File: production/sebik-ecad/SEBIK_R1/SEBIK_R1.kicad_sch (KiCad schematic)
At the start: 59 parts

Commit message: updated schematic with usb port, test points, and mounting holes
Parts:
- removed FB? (x6): FerriteBead, symbol Device:FerriteBead
- removed J? (x2): Conn_01x02_Male, Connector_JST:JST_XH_B2B-XH-AM_1x02_P2.50mm_Vertical, symbol Connector:Conn_01x02_Male
- added C?: 100n, Capacitor_SMD:C_0805_2012Metric, symbol Device:C_Small
- added D? (x2): LED_Small, LED_SMD:LED_0805_2012Metric, symbol Device:LED_Small
- added E1, E2, E3, E4, E5, E6: MI0805K400R-10, MI0805K400R-10:FB_MI0805K400R-10, symbol MI0805K400R-10:MI0805K400R-10
- added F?: 500mA, Fuse:Fuse_1210_3225Metric, symbol Device:Fuse
- added H1, H2, H3, H4: MountingHole, MountingHole:MountingHole_3.2mm_M3, symbol Mechanical:MountingHole
- added J8, J9: Conn_01x01_Male, Connector_JST:JST_XH_B1B-XH-AM_1x01_P2.50mm_Vertical, symbol Connector:Conn_01x01_Male
- added J?: USB_B, Connector_USB:USB_Micro-B_Amphenol_10104110_Horizontal, symbol Connector:USB_B
- added R?: 10k, Resistor_SMD:R_0805_2012Metric, symbol Device:R_Small
- added R? (x5): 1k, Resistor_SMD:R_0805_2012Metric, symbol Device:R_Small
- added TP? (x2): TestPoint, TestPoint:TestPoint_Loop_D1.80mm_Drill1.0mm_Beaded, symbol Connector:TestPoint
- added U3: USBLC6-2SC6, Package_TO_SOT_SMD:SOT-23-6, symbol Power_Protection:USBLC6-2SC6
- added U4: FT232RL, Package_SO:SSOP-28_5.3x10.2mm_P0.65mm, symbol Interface_USB:FT232RL
- D?: footprint Diode_THT:D_DO-35_SOD27_P7.62mm_Horizontal -> Diode_SMD:D_0805_2012Metric
- D?: footprint (none) -> Diode_SMD:D_0805_2012Metric
- gave numbers to parts that had none: 17
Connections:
- net +5V: now also R?.1, R?.2, R?.2, TP?.1, U4.20 (VCC), U4.4 (VCCIO)
- net GND: now also C?.2, J?.4 (GND), R?.1, U3.2 (GND), U4.18 (GND), U4.21 (GND), U4.25 (AGND), U4.26 (TEST), U4.7 (GND)
- net at C?.1, U7.2 (T-): now also E5.2
- net at C?.2, U7.3 (T+): now also E6.2
- net at J5.1 (Pin_1): now also E1.1
- net at J5.2 (Pin_2): now also E2.1
- net at C?.2, U5.3 (T+): now also E2.2
- net at C?.1, U5.2 (T-): now also E1.2
- net at Q2.3 (D): now also J8.1 (Pin_1)
- net RX: now reaches U1.30 (PD0)
- net RX: now also R?.2
- net TX: now reaches U1.31 (PD1)
- net TX: now also R?.2
- net at J10.1 (Pin_1): now also E5.1
- net at Q1.3 (D): now also J9.1 (Pin_1)
- net at J6.1 (Pin_1): now also E3.1
- net at C?.1, U6.2 (T-): now also E3.2
- net at C?.2, U6.3 (T+): now also E4.2
- net at J6.2 (Pin_2): now also E4.1
- net at J10.2 (Pin_2): now also E6.1
- new net: R?.2, U4.19 (~{RESET})
- new net: D?.2 (A), R?.1 (x2)
- new net: R?.1, U4.1 (TXD)
- new net: D?.1 (K), U4.22 (CBUS1)
- new net: D?.1 (K), U4.23 (CBUS0)
- new net: R?.1, U4.5 (RXD)
- new net: F?.1, J?.1 (VBUS)
- new net +3V3: C?.1, TP?.1, U4.17 (3V3OUT)
- new net DTR: R?.2, U4.2 (DTR)
- new net USB_CON_D+: J?.3 (D+), U3.1 (I/O1)
- new net USB_CON_D-: J?.2 (D-), U3.3 (I/O2)
- new net USB_D+: U3.6 (I/O1), U4.15 (USBD+)
- new net USB_D-: U3.4 (I/O2), U4.16 (USBD-)
- new net VBUS: F?.2, U3.5 (VBUS)
- no-connect marks 0 -> 11
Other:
- note added: "GPIO Expander"
- note added: "MOUNTING HOLES"
- note added: "Microcontroller"
- note added: "USB"
- moved on the sheet: C?, D?, J1, J10, J11, J2, J3, J4, J5, J6, J7, J?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

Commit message: added non power net test points, numbered all parts and added crystal and switch footprints
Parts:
- removed D?: LED, LED_SMD:LED_0805_2012Metric, symbol Device:LED
- removed J?: 0, symbol test:3pin-I/O
- removed R?: 10k, Resistor_SMD:R_0805_2012Metric, symbol Device:R_Small
- removed R? (x5): 1k, Resistor_SMD:R_0805_2012Metric, symbol Device:R_Small
- removed R?: 1K, Resistor_SMD:R_0805_2012Metric, symbol Device:R_US
- added J12: Conn_01x02_Male, Connector_JST:JST_XH_B2B-XH-AM_1x02_P2.50mm_Vertical, symbol Connector:Conn_01x02_Male
- added R10, R11, R12, R13, R14: 1K, Resistor_SMD:R_0805_2012Metric, symbol Device:R_US
- added R9: 10k, Resistor_SMD:R_0805_2012Metric, symbol Device:R_US
- added TP_MISO, TP_SCK, TP_ej_press, TP_ej_sol_in, TP_inj_press, TP_inj_sol_in, TP_speaker: TestPoint, TestPoint:TestPoint_Loop_D1.80mm_Drill1.0mm_Beaded, symbol Connector:TestPoint
- SW?: footprint (none) -> Button_Switch_SMD:SW_SPDT_PCM12
- Y1: renamed from Y?; footprint (none) -> Crystal:Crystal_SMD_2012-2Pin_2.0x1.2mm
- gave numbers to parts that had none: 33
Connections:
- net +5V: now also R13.2, R14.2, R9.2
- net DTR: now also R12.2
- net GND: now also R12.1
- net RX: now also R11.1
- net SCK: now also TP_SCK.1
- net Speaker: now also TP_speaker.1
- net TX: now also R10.1
- net ej_press: now also TP_ej_press.1
- net ej_sol_in: now also TP_ej_sol_in.1
- net inj_press: now also TP_inj_press.1
- net inj_sol_in: now also TP_inj_sol_in.1
- net at U4.19 (~{RESET}): now also R9.1
- net at D7.2 (A): now also R13.1
- net at U4.1 (TXD): now also R10.2
- net at D8.2 (A): now also R14.1
- net at U4.5 (RXD): now also R11.2
- net at K?.14: now also J12.2 (Pin_2)
- net at K?.7, K?.8: now also J12.1 (Pin_1)
- net MISO: now reaches U1.16 (PB4)
- net MISO: now also U5.7 (SO), U6.7 (SO), U7.7 (SO), TP_MISO.1
- removed net MOSI: U1.15 (PB3), U5.7 (SO), U6.7 (SO), U7.7 (SO)
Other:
- note added: "2012"
- moved on the sheet: D7, D8, Q3, R7, R8

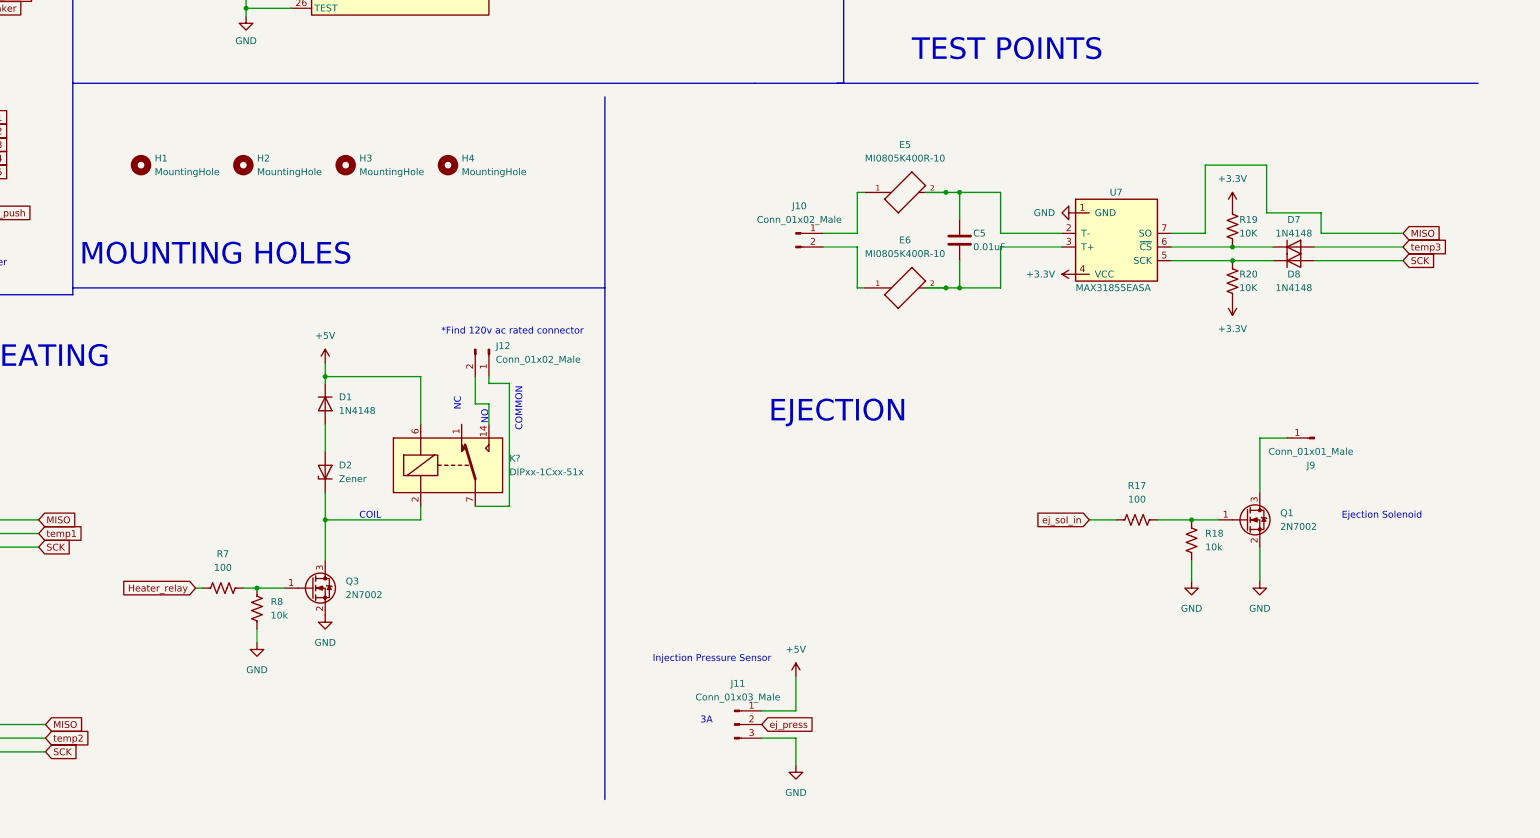
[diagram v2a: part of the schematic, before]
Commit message: added mounting holes for buck converter and connector for 5v from buck
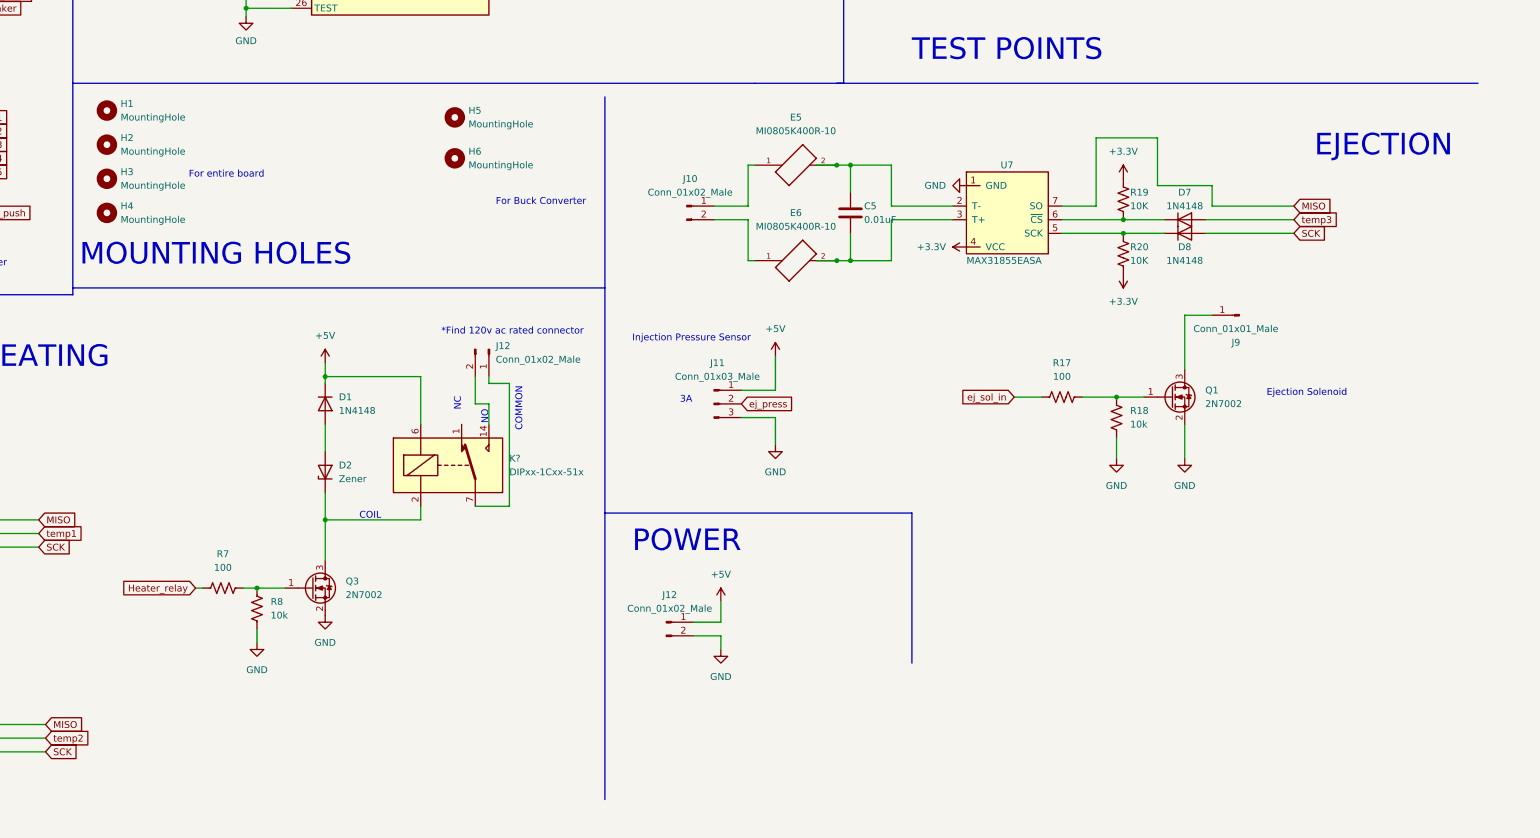
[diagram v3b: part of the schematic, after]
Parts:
- added H5, H6: MountingHole, MountingHole:MountingHole_3.2mm_M3, symbol Mechanical:MountingHole
- added J12: Conn_01x02_Male, Connector_JST:JST_XH_B2B-XH-AM_1x02_P2.50mm_Vertical, symbol Connector:Conn_01x02_Male
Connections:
- net +5V: now also J12.1 (Pin_1)
- net GND: now also J12.2 (Pin_2)
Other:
- note added: "For Buck Converter"
- note added: "For entire board"
- note added: "POWER"
- moved on the sheet: C5, D7, D8, E5, E6, H1, H2, H3, H4, J10, J11, J9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

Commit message: added connector for relay to shut down power
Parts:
- added J13: Conn_01x02_Male, Connector_JST:JST_XH_B2B-XH-AM_1x02_P2.50mm_Vertical, symbol Connector:Conn_01x02_Male
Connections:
- net GND: now also J13.1 (Pin_1)
- net stop_relay: now reaches U2.3 (GPB2)
- net stop_relay: now also J13.2 (Pin_2)
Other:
- moved on the sheet: J4
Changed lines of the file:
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@@
     (stroke (width 0) (type default) (color 0 0 0 0))
   )
-  (wire (pts (xy 74.93 54.61) (xy 72.39 54.61))
+  (wire (pts (xy 80.01 58.42) (xy 77.47 58.42))
     (stroke (width 0) (type default) (color 0 0 0 0))
   )
@@
     (stroke (width 0) (type default) (color 0 0 0 0))
   )
+  (wire (pts (xy 74.93 44.45) (xy 74.93 46.99))
+    (stroke (width 0) (type default) (color 0 0 0 0))
+  )
   (wire (pts (xy 105.41 231.14) (xy 113.03 231.14))
     (stroke (width 0) (type default) (color 0 0 0 0))
@@
     (stroke (width 0) (type default) (color 0 0 0 0))
   )
-  (wire (pts (xy 72.39 54.61) (xy 72.39 57.15))
+  (wire (pts (xy 77.47 58.42) (xy 77.47 60.96))
     (stroke (width 0) (type default) (color 0 0 0 0))
   )
@@
     (stroke (width 0) (type default) (color 0 0 0 0))
   )
+  (wire (pts (xy 77.47 44.45) (xy 74.93 44.45))
+    (stroke (width 0) (type default) (color 0 0 0 0))
+  )
   (wire (pts (xy 281.94 160.02) (xy 285.75 160.02))
     (stroke (width 0) (type default) (color 0 0 0 0))
@@
     (stroke (width 0) (type default) (color 0 0 0 0))
   )
-  (wire (pts (xy 71.12 52.07) (xy 74.93 52.07))
+  (wire (pts (xy 76.2 55.88) (xy 80.01 55.88))
     (stroke (width 0) (type default) (color 0 0 0 0))
   )
@@
     (stroke (width 0) (type default) (color 0 0 0 0))
   )
+  (wire (pts (xy 73.66 41.91) (xy 77.47 41.91))
+    (stroke (width 0) (type default) (color 0 0 0 0))
+  )
   (wire (pts (xy 274.32 195.58) (xy 274.32 201.93))
     (stroke (width 0) (type default) (color 0 0 0 0))
@@
     )
   )
+  (global_label "stop_relay" (shape input) (at 73.66 41.91 180) (fields_autoplaced)
+    (effects (font (size 1.27 1.27)) (justify right))
+    (property "Intersheet References" "${INTERSHEET_REFS}" (id 0) (at 61.5707 41.8306 0)
+      (effects (font (size 1.27 1.27)) (justify right) hide)
+    )
+  )
   (global_label "ej_press" (shape input) (at 46.99 129.54 0) (fields_autoplaced)
     (effects (font (size 1.27 1.27)) (justify left))
@@
     )
   )
-  (global_label "stop_push" (shape input) (at 71.12 52.07 180) (fields_autoplaced)
+  (global_label "stop_push" (shape input) (at 76.2 55.88 180) (fields_autoplaced)
     (effects (font (size 1.27 1.27)) (justify right))
-    (property "Intersheet References" "${INTERSHEET_REFS}" (id 0) (at 59.2121 51.9906 0)
+    (property "Intersheet References" "${INTERSHEET_REFS}" (id 0) (at 64.2921 55.8006 0)
       (effects (font (size 1.27 1.27)) (justify right) hide)
     )
@@
     )
   )
+  (global_label "stop_relay" (shape input) (at 124.46 133.35 0) (fields_autoplaced)
+    (effects (font (size 1.27 1.27)) (justify left))
+    (property "Intersheet References" "${INTERSHEET_REFS}" (id 0) (at 136.5493 133.2706 0)
+      (effects (font (size 1.27 1.27)) (justify left) hide)
+    )
+  )
   (symbol (lib_id "power:VBUS") (at 155.702 33.02 0) (unit 1)
     (in_bom yes) (on_board yes) (fields_autoplaced)
@@
     (pin "1")
   )
+  (symbol (lib_id "Connector:Conn_01x02_Male") (at 82.55 44.45 180) (unit 1)
+    (in_bom yes) (on_board yes) (fields_autoplaced)
+    (property "Reference" "J13" (id 0) (at 83.82 41.9099 0)
+      (effects (font (size 1.27 1.27)) (justify right))
+    )
+    (property "Value" "Conn_01x02_Male" (id 1) (at 83.82 44.4499 0)
+      (effects (font (size 1.27 1.27)) (justify right))
+    )
+    (property "Footprint" "Connector_JST:JST_XH_B2B-XH-AM_1x02_P2.50mm_Vertical" (id 2) (at 82.55 44.45 0)
+      (effects (font (size 1.27 1.27)) hide)
+    )
+    (property "Datasheet" "~" (id 3) (at 82.55 44.45 0)
+      (effects (font (size 1.27 1.27)) hide)
+    )
+    (pin "1")
+    (pin "2")
+  )
   (symbol (lib_id "Device:LED_Small") (at 252.73 116.84 90) (unit 1)
     (in_bom yes) (on_board yes) (fields_autoplaced)
@@
     (pin "1")
   )
-  (symbol (lib_id "power:GND") (at 72.39 57.15 0) (unit 1)
+  (symbol (lib_id "power:GND") (at 77.47 60.96 0) (unit 1)
     (in_bom yes) (on_board yes) (fields_autoplaced)
-    (property "Reference" "#PWR?" (id 0) (at 72.39 63.5 0)
+    (property "Reference" "#PWR?" (id 0) (at 77.47 67.31 0)
       (effects (font (size 1.27 1.27)) hide)
     )
-    (property "Value" "GND" (id 1) (at 72.39 62.23 0))
-    (property "Footprint" "" (id 2) (at 72.39 57.15 0)
+    (property "Value" "GND" (id 1) (at 77.47 66.04 0))
+    (property "Footprint" "" (id 2) (at 77.47 60.96 0)
       (effects (font (size 1.27 1.27)) hide)
     )
-    (property "Datasheet" "" (id 3) (at 72.39 57.15 0)
+    (property "Datasheet" "" (id 3) (at 77.47 60.96 0)
       (effects (font (size 1.27 1.27)) hide)
     )
@@
     (pin "1")
   )
-  (symbol (lib_id "Connector:Conn_01x02_Male") (at 80.01 54.61 180) (unit 1)
+  (symbol (lib_id "Connector:Conn_01x02_Male") (at 85.09 58.42 180) (unit 1)
     (in_bom yes) (on_board yes) (fields_autoplaced)
-    (property "Reference" "J4" (id 0) (at 81.28 52.0699 0)
+    (property "Reference" "J4" (id 0) (at 86.36 55.8799 0)
       (effects (font (size 1.27 1.27)) (justify right))
     )
-    (property "Value" "Conn_01x02_Male" (id 1) (at 81.28 54.6099 0)
+    (property "Value" "Conn_01x02_Male" (id 1) (at 86.36 58.4199 0)
       (effects (font (size 1.27 1.27)) (justify right))
     )
-    (property "Footprint" "Connector_JST:JST_XH_B2B-XH-AM_1x02_P2.50mm_Vertical" (id 2) (at 80.01 54.61 0)
+    (property "Footprint" "Connector_JST:JST_XH_B2B-XH-AM_1x02_P2.50mm_Vertical" (id 2) (at 85.09 58.42 0)
       (effects (font (size 1.27 1.27)) hide)
     )
-    (property "Datasheet" "~" (id 3) (at 80.01 54.61 0)
+    (property "Datasheet" "~" (id 3) (at 85.09 58.42 0)
       (effects (font (size 1.27 1.27)) hide)
     )
@@
     (pin "1")
   )
+  (symbol (lib_id "power:GND") (at 74.93 46.99 0) (unit 1)
+    (in_bom yes) (on_board yes)
+    (property "Reference" "#PWR?" (id 0) (at 74.93 53.34 0)
+      (effects (font (size 1.27 1.27)) hide)
+    )
+    (property "Value" "GND" (id 1) (at 74.93 50.8 0))
+    (property "Footprint" "" (id 2) (at 74.93 46.99 0)
+      (effects (font (size 1.27 1.27)) hide)
+    )
+    (property "Datasheet" "" (id 3) (at 74.93 46.99 0)
+      (effects (font (size 1.27 1.27)) hide)
+    )
+    (pin "1")
+  )
   (symbol (lib_id "power:+3V3") (at 154.432 80.01 0) (unit 1)
     (in_bom yes) (on_board yes) (fields_autoplaced)
@@
       (reference "#PWR?") (unit 1) (value "+3.3V") (footprint "")
     )
+    (path "/a392439e-ad07-4e12-8535-bc3711d6b8bb"
+      (reference "#PWR?") (unit 1) (value "GND") (footprint "")
+    )
     (path "/a74415a8-0bc8-4672-bc4c-d979a1a1cccb"
       (reference "#PWR?") (unit 1) (value "+3V3") (footprint "")
@@
       (reference "J12") (unit 1) (value "Conn_01x02_Male") (footprint "Connector_JST:JST_XH_B2B-XH-AM_1x02_P2.50mm_Vertical")
     )
+    (path "/3f6c2852-cd98-4780-842e-39ca2bba6a1a"
+      (reference "J13") (unit 1) (value "Conn_01x02_Male") (footprint "Connector_JST:JST_XH_B2B-XH-AM_1x02_P2.50mm_Vertical")
+    )
     (path "/6fe48f1e-4227-4f41-a8f4-0e7ec51a11e0"

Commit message: Addressed comments from Nick
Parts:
- removed F1: 500mA, Fuse:Fuse_1210_3225Metric, symbol Device:Fuse
- removed J1: Conn_01x06_Male, Connector_JST:JST_XH_B6B-XH-AM_1x06_P2.50mm_Vertical, symbol Connector:Conn_01x06_Male
- removed J11: USB_B, Connector_USB:USB_Micro-B_Amphenol_10104110_Horizontal, symbol Connector:USB_B
- added F?: 500mA, Fuse:Fuse_1210_3225Metric, symbol Device:Fuse
- added J?: Conn_01x05_Male, symbol Connector:Conn_01x05_Male
- added P?: USB_C_Plug, symbol Connector:USB_C_Plug
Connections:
- net GND: now also J?.5 (Pin_5), P?.A1 (GND), P?.A12 (GND), P?.B1 (GND), P?.B12 (GND)
- net USB_CON_D+: now also P?.A6 (D+)
- net USB_CON_D-: now also P?.A7 (D-)
- net VBUS: now also F?.2
- new net: F?.1, P?.A4 (VBUS), P?.A9 (VBUS), P?.B4 (VBUS), P?.B9 (VBUS)
- new net High Pressure/Complete Yellow LED: J?.1 (Pin_1)
- new net High Temp Yellow LED: J?.4 (Pin_4)
- new net In Progress Yellow LED: J?.3 (Pin_3)
- new net Low Temp Yellow LED: J?.2 (Pin_2)
- no-connect marks 11 -> 23
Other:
- note added: "LED Board"
- moved on the sheet: C6, D7, D8, J13, J2, J4, R10, R11, R12, R13, R14, R9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
